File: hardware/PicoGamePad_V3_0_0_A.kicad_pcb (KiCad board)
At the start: 4 copper layers, 68.9 x 37.6 mm, 54 parts, among them J1 C116159, J3 RBP_GPIO_CONN, SW1 DOWN, SW2 START, SW3 LEFT, SW4 B, SW5 UP, SW6 A, SW7 RIGHT, SW8 SELECT, U1 ASM1117-3.3, U3 WQ25JVS, U4 RP2040, Y1 X322512MMB4SI

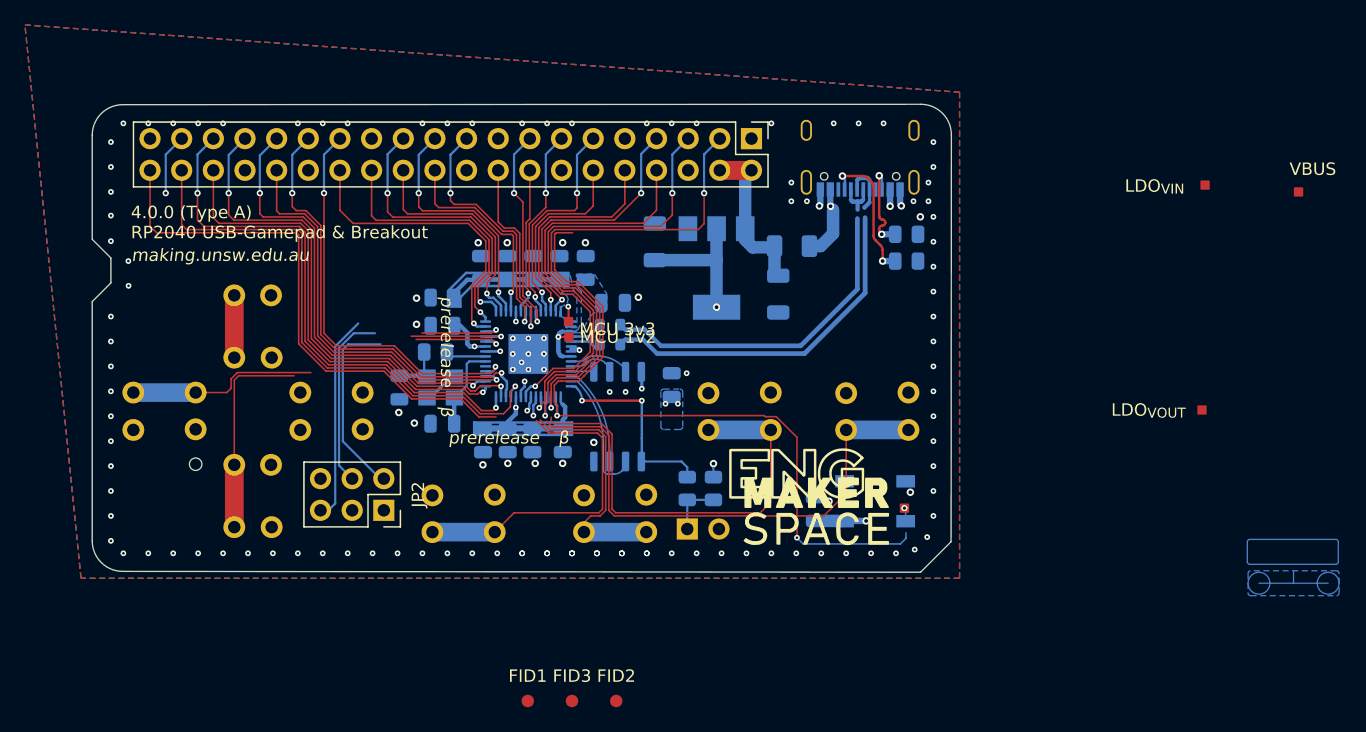
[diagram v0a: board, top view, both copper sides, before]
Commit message: 
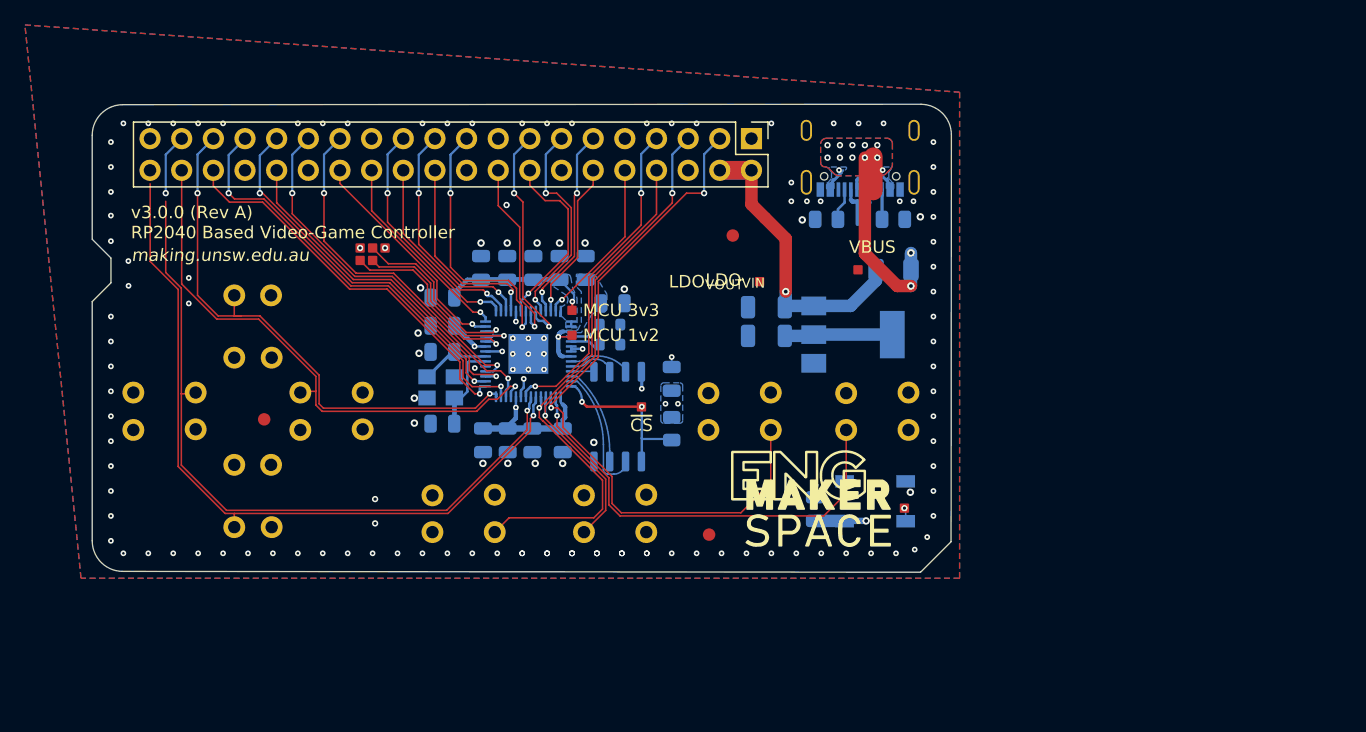
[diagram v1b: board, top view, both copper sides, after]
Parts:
- removed ?: , 
- removed JP1: Conn_01x02, Connector_PinSocket_2.54mm:PinSocket_1x02_P2.54mm_Vertical
- removed JP2: Conn_02x03, Connector_PinSocket_2.54mm:PinSocket_2x03_P2.54mm_Vertical
- removed R4: R, Resistor_SMD:R_0805_2012Metric
- removed R7: 1k?, Resistor_SMD:R_0805_2012Metric
- added TP11: SWD_3V3, 0:Testpoint_Custom, F.Cu at (113.5, 66.5)
- added TP12: ~{CS}, 0:Testpoint_Custom, F.Cu at (134.1, 79.2)
- added TP3: RUN, 0:Testpoint_Custom, F.Cu at (112.5, 66.5)
- added TP4: SWCLK, 0:Testpoint_Custom, F.Cu at (111.5, 67.5)
- added TP6: SWD, 0:Testpoint_Custom, F.Cu at (112.5, 67.5)
- added TP7: RUN_GND, 0:Testpoint_Custom, F.Cu at (111.5, 66.5)
- SW1: value DOWN -> SW_Push
- SW2: value START -> SW_Push
- SW3: value LEFT -> SW_Push
- SW4: value B -> SW_Push
- SW5: value UP -> SW_Push
- SW6: value A -> SW_Push
- SW7: value RIGHT -> SW_Push
- SW8: value SELECT -> SW_Push
- moved FID3 39.5 mm to (141.4, 65.5)
- moved TP9 37.0 mm to (143.6, 69.2)
- moved TP8 35.9 mm to (151.4, 68.2)
- moved TP10 34.5 mm to (145.7, 69.0)
- moved FID1 31.0 mm to (103.8, 80.2)
- moved FID2 15.3 mm to (139.5, 89.5)
- moved U1 12.2 mm to (151.1, 73.5), turned to 0 degrees
- moved C3 11.7 mm to (144.1, 73.5), turned to 180 degrees
- moved F1 8.37 mm to (154.3, 68.2)
- moved R5 7.25 mm to (148.9, 64.2), turned to 180 degrees
- moved R6 5.85 mm to (136.5, 81.0)
- moved C6 4.48 mm to (118.1, 74.8), turned to 180 degrees
- moved C9 3.56 mm to (131.8, 70.9), turned to 0 degrees
- moved C8 3.56 mm to (129.6, 68.1), turned to 90 degrees
- moved R1 1.60 mm to (154.3, 64.2)
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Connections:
- R6 pad 1: Net-(R6-Pad1) -> /~{CS}
- U4 pad 21: Net-(U4-Pad21) -> Net-(C6-Pad1)
- U4 pad 24: /SWCLK -> Net-(TP4-Pad1)
- U4 pad 25: /SWD/SWDIO -> Net-(TP6-Pad1)
- U4 pad 26: /~{RESET}/RUN -> Net-(TP3-Pad1)
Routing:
- net /$.GPIO0: track 101.6 -> 35.7 mm, vias 2 -> 1
- net /$.GPIO4: track 23.2 -> 65.1 mm
- net /USB_{DATA}+: track 32.6 -> 5.56 mm
- net /USB_{DATA}-: track 30.7 -> 4.55 mm
- net /~{RESET}/RUN: track 23.6 -> 0.00 mm, vias 1 -> 0
- net /SWD/SWDIO: track 22.8 -> 0.00 mm, vias 1 -> 0
- net /SWCLK: track 22.6 -> 0.00 mm, vias 1 -> 0
- net /$.GPIO1: track 75.2 -> 57.2 mm
- net /$.GPIO2: track 57.8 -> 40.5 mm
- net Net-(TP4-Pad1): track 0.00 -> 15.5 mm, vias 0 -> 1
- net Net-(TP6-Pad1): track 0.00 -> 15.4 mm, vias 0 -> 1
- net /$.GPIO3: track 58.9 -> 43.6 mm
- net Net-(TP3-Pad1): track 0.00 -> 14.6 mm, vias 0 -> 1
- net /USB_VBUS: track 11.7 -> 22.1 mm, vias 2 -> 14
- net VBUS: track 20.2 -> 30.5 mm, vias 1 -> 2
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- added copper zone on B.Cu, net /USB_VBUS
- added copper zone on F.Cu, net /USB_VBUS
- removed copper zone on B.Cu, net (none)
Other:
- rule pad_to_mask_clearance: 0.05 -> 0
- board text added: "v3.0.0 (Rev A) RP2040 Based Video-Game Controller"
- board text removed: "${REVISION} RP2040 USB-Gamepad & Breakout"
- board text removed: "prerelease"
- board text removed: "β"
